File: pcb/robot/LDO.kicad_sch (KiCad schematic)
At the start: 19 parts, among them U14 MAX77642ANA+

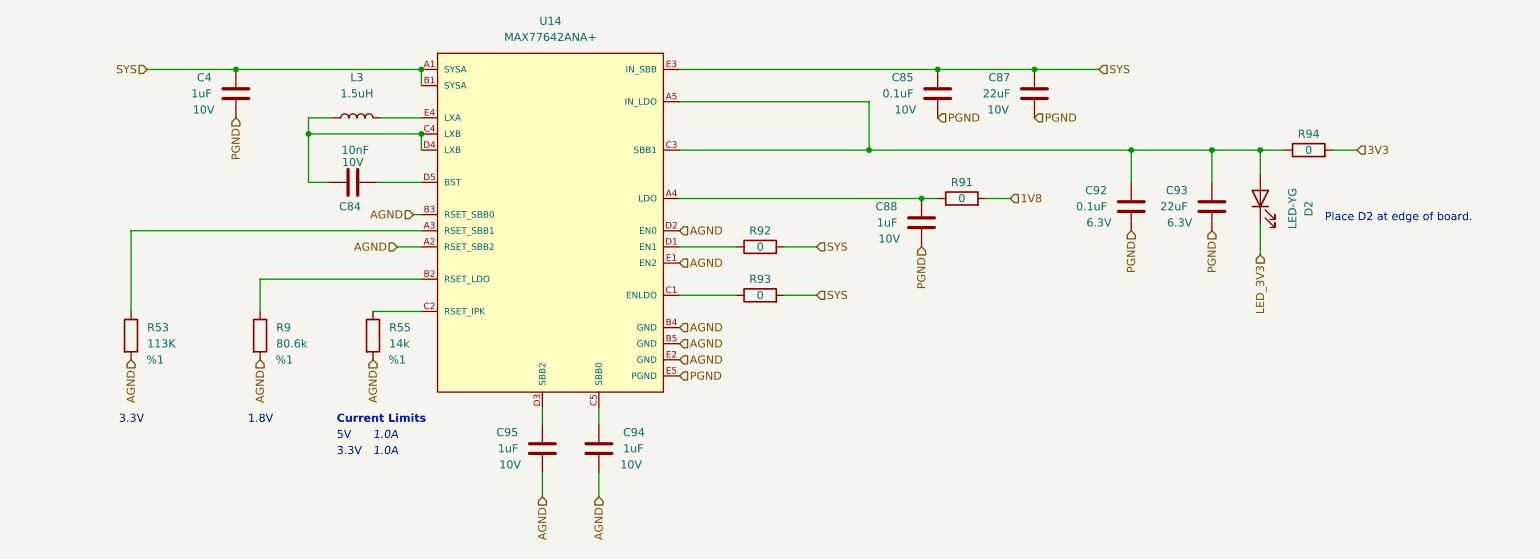
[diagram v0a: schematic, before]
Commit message: Modification and replacement of MAX77642ANA
The MAX77642ANA was replaced with the LDO XC6206 and the TPS63021DSJR. Rerouting and Gerber updates were performed.
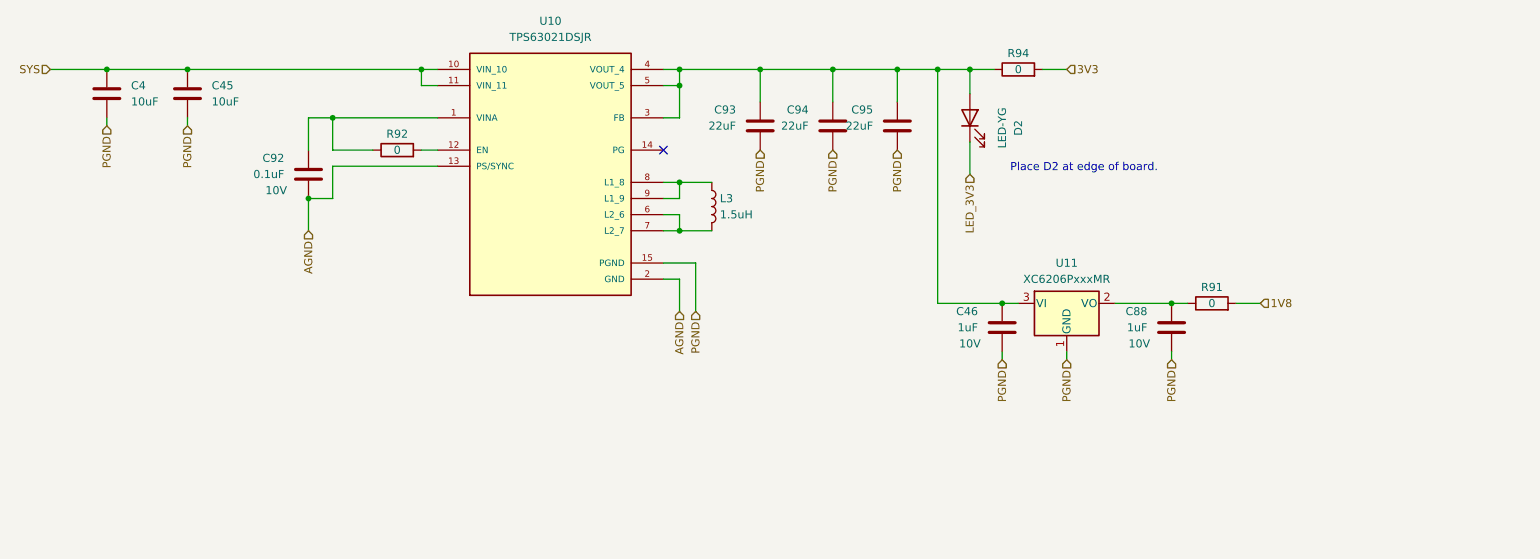
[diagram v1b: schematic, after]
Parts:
- removed C84: 10nF, robot:C_0402_1005Metric, symbol robot:C
- removed C85: 0.1uF, robot:C_0402_1005Metric, symbol robot:C
- removed C87: 22uF, robot:C_0603_1608Metric, symbol robot:C
- removed R53: 113K, robot:R_0603_1608Metric, symbol robot:R
- removed R55: 14k, robot:R_0603_1608Metric, symbol robot:R
- removed R9: 80.6k, robot:R_0402_1005Metric, symbol robot:R
- removed R93: 0, robot:R_0603_1608Metric, symbol Device:R
- removed U14: MAX77642ANA+, robot:Maxim-N252B2-1-0-A-MFG, symbol robot:MAX77642ANA+
- added C45: 10uF, robot:C_0603_1608Metric, symbol robot:C
- added C46: 1uF, robot:C_0402_1005Metric, symbol robot:C
- added U10: TPS63021DSJR, robot:IC_TPS63021DSJR, symbol robot:TPS63021DSJR
- added U11: XC6206PxxxMR, Package_TO_SOT_SMD:SOT-23-3, symbol Regulator_Linear:XC6206PxxxMR
- C4: value 1uF -> 10uF; footprint robot:C_0402_1005Metric -> robot:C_0603_1608Metric; Part Number GRM155R61E105KA12D -> GRM188R61E106KA73J; Stock 10 -> (none); V_Max (none) -> 25V
- C94, C95: value 1uF -> 22uF; footprint robot:C_0402_1005Metric -> robot:C_0603_1608Metric; Part Number GRM155R61E105KA12D -> GRM188R61A226ME15D; Stock 10 -> (none)
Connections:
- net AGND: now also C92.2, U10.13 (PS/SYNC), U10.2 (GND); no longer C94.2, C95.2
- net PGND: now also C4.1, C94.2, C95.2, C45.1, C46.2, U10.15 (PGND), U11.1 (GND); no longer C4.2, C92.2
- net SYS: now also C4.2, C45.2, U10.10 (VIN_10), U10.11 (VIN_11); no longer C4.1, R92.2
- net at C93.1, D2.2 (A), R94.1: now also C94.1, C95.1, C46.1, U10.3 (FB), U10.4 (VOUT_4), U10.5 (VOUT_5), U11.3 (VI); no longer C92.1
- net at C88.1, R91.1: now also U11.2 (VO)
- net at L3.1: now also U10.8 (L1_8), U10.9 (L1_9)
- net at L3.2: now also U10.6 (L2_6), U10.7 (L2_7)
- net at R92.1: now also C92.1, U10.1 (VINA)
- new net: R92.2, U10.12 (EN)
- no-connect marks 0 -> 1
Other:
- note removed: "1.0A"
- note removed: "1.8V"
- note removed: "3.3V"
- note removed: "5V"
- note removed: "Current Limits"
- moved on the sheet: C88, C93, D2, L3, R91, R92, R94
